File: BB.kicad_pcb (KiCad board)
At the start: 2 copper layers, 0 parts

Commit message: Added Relay module footprints.
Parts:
- added D1: LG Q971-KN-1, LEDs:LED-0603, F.Cu at (300.1, 95.9)
- added D2: B130-13-F, BB:SMA, F.Cu at (296.7, 104.0)
- added K1: 1461069-5, BB:TE-SPDT, F.Cu at (306.4, 96.6)
- added Q1: 2N3904, SMD_Packages:SOT23EBC, B.Cu at (304.5, 103.4)
- added R1: 500, SMD_Packages:SM0805, F.Cu at (290.6, 90.9)
- added R2: 200, SMD_Packages:SM0805, F.Cu at (300.6, 99.7)
- added R3: 100, SMD_Packages:SM0805, B.Cu at (307.0, 93.6)
- added R4: 0, SMD_Packages:SM0805, B.Cu at (305.4, 89.3)
- added R5: 0, SMD_Packages:SM0805, B.Cu at (312.5, 90.0)
- added R6: 0, SMD_Packages:SM0805, B.Cu at (304.3, 99.2)
- added U1: LTV-816S, BB:4-SMD, F.Cu at (293.2, 90.2)
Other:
- board outline added: 165.1 x 63.5 mm
- copper layers 2 -> 4
- rule pad_to_mask_clearance: 0 -> 0.127
- rule trace_min: 0.254 -> 0.1524
- rule via_min_drill: 0.508 -> 0.3302
- rule via_min_size: 0.889 -> 0.508

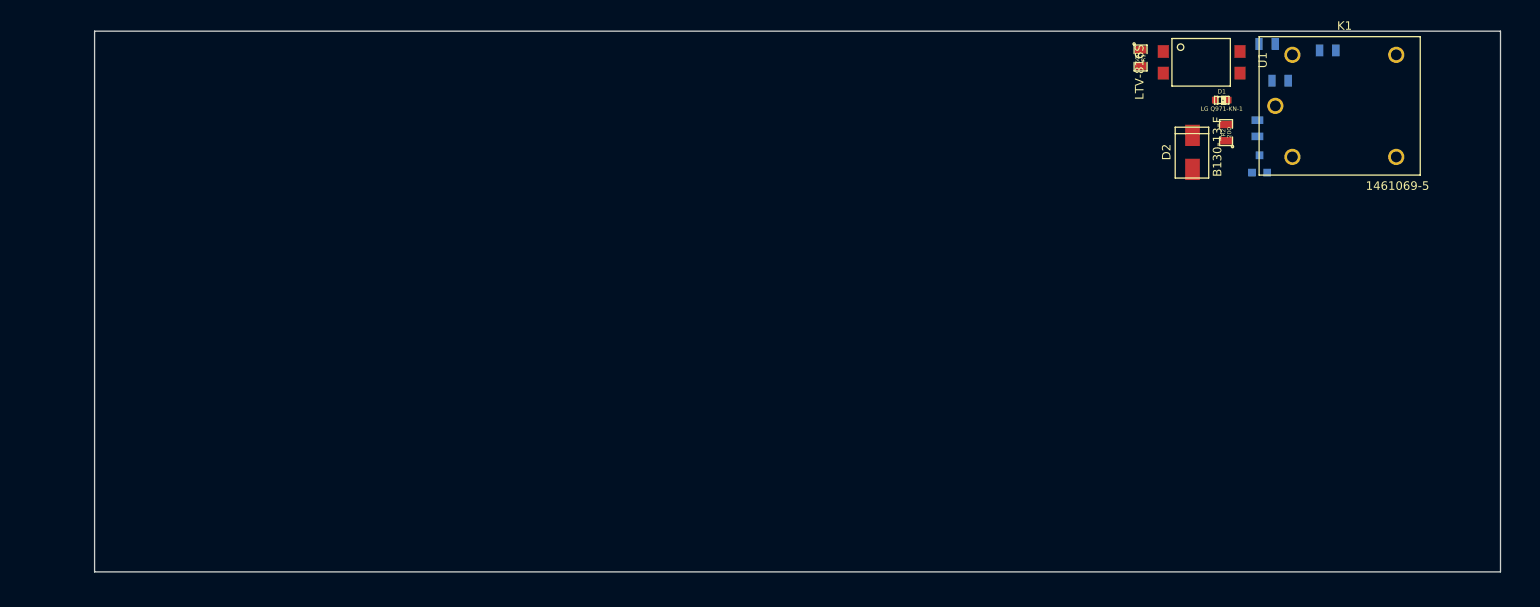
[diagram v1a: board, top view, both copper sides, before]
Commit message: Associated and placed thermocouple, terminal, arduino, fan driver, power protection modules.
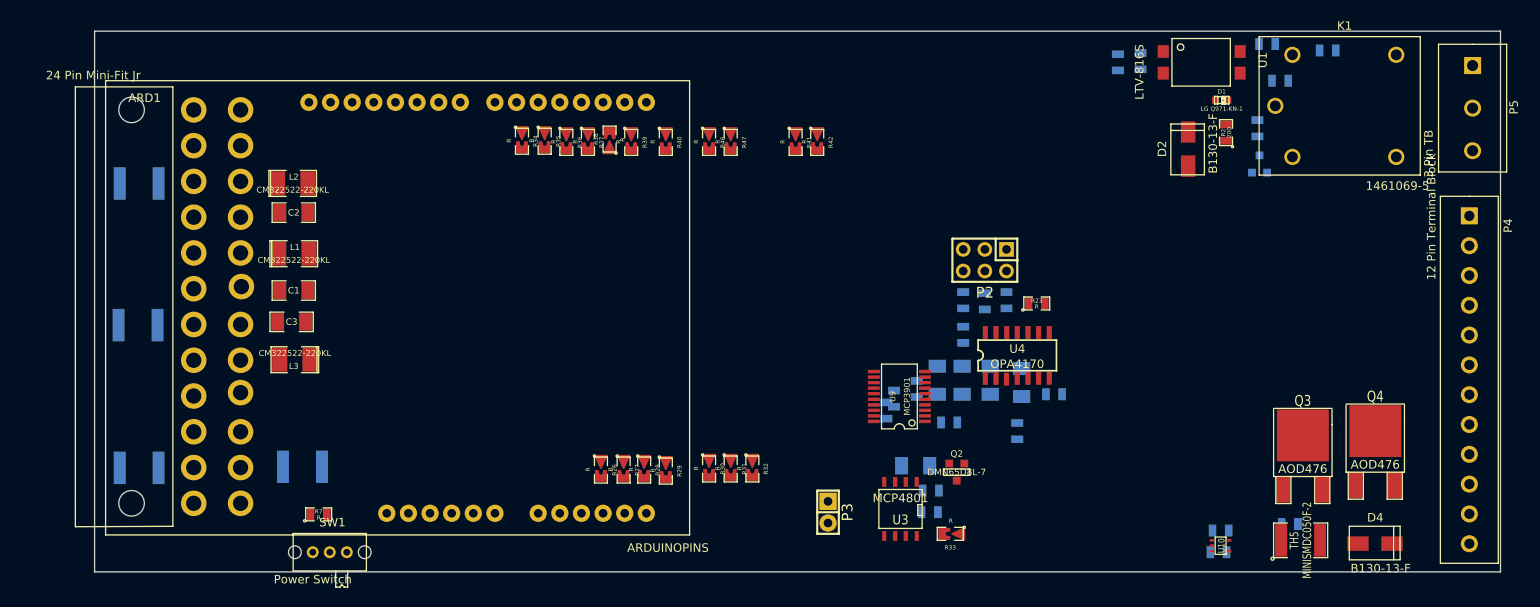
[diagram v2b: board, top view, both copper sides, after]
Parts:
- added ARD1: ARDUINOPINS, BB:Arduino, F.Cu at (203.6, 120.5)
- added C1: C, SMD_Packages:SM1206, F.Cu at (191.1, 118.2)
- added C10: C, SMD_Packages:SM0805, B.Cu at (276.1, 134.7)
- added C11: C, SMD_Packages:SM0805, B.Cu at (299.7, 149.0)
- added C12: C, SMD_Packages:SM0805, B.Cu at (265.9, 141.7)
- added C13: C, SMD_Packages:SM0805, B.Cu at (308.1, 145.7)
- added C2: C, SMD_Packages:SM1206, F.Cu at (191.1, 109.1)
- added C3: C, SMD_Packages:SM1206, F.Cu at (190.9, 121.9)
- added C6: C, SMD_Packages:SM0805, B.Cu at (264.3, 129.8)
- added C7: C, SMD_Packages:SM0805, B.Cu at (261.6, 130.9)
- added C8: C, SMD_Packages:SM0805, B.Cu at (260.7, 132.3)
- added C9: C, SMD_Packages:SM0805, B.Cu at (280.4, 130.4)
- added D4: B130-13-F, BB:SMA, F.Cu at (316.1, 148.0)
- added L1: CM322522-220KL, SMD_Packages:SM1210L, F.Cu at (191.1, 113.9)
- added L2: CM322522-220KL, SMD_Packages:SM1210L, F.Cu at (191.0, 105.7)
- added L3: CM322522-220KL, SMD_Packages:SM1210L, F.Cu at (191.3, 126.4)
- added P1: 24 Pin Mini-Fit Jr, BB:ATX_Header, F.Cu at (172.1, 97.0)
- added P2: CONN_3X2, BB:Pin_Header_Straight_3X2, F.Cu at (272.3, 114.7)
- added P3: CONN_2, Pin_Headers:Pin_Header_Straight_1x02, F.Cu at (253.9, 144.3)
- added P4: 12 Pin Terminal Block, BB:12PinTB, F.Cu at (329.2, 109.5)
- added P5: 3 Pin TB, BB:3PinTB, F.Cu at (329.6, 91.8)
- added Q2: DMN65D8L-7, SMD_Packages:SOT23GDS, F.Cu at (269.0, 139.6)
- added Q3: AOD476, SMD_Packages:DPAK2, F.Cu at (309.6, 141.6)
- added Q4: AOD476, SMD_Packages:DPAK2, F.Cu at (318.1, 141.1)
- added R10: R, SMD_Packages:SM1206, B.Cu at (264.2, 138.8)
- added R19: R, SMD_Packages:SM1206, B.Cu at (276.6, 129.0)
- added R20: R, SMD_Packages:SM1206, B.Cu at (266.7, 128.8)
- added R21: R, SMD_Packages:SM1206, B.Cu at (272.9, 128.8)
- added R22: R, SMD_Packages:SM1206, B.Cu at (269.6, 128.8)
- added R23: R, SMD_Packages:SM0805, F.Cu at (278.4, 119.8)
- added R24: R, SMD_Packages:SM0805, B.Cu at (269.7, 119.4)
- added R25: R, SMD_Packages:SM0805, B.Cu at (269.7, 123.4)
- added R26: R, BB:SM0805-blob, F.Cu at (227.2, 139.3)
- added R27: R, BB:SM0805-blob, F.Cu at (229.9, 139.3)
- added R28: R, BB:SM0805-blob, F.Cu at (232.3, 139.3)
- added R29: R, BB:SM0805-blob, F.Cu at (234.8, 139.4)
- added R30: R, BB:SM0805-blob, F.Cu at (239.9, 139.2)
- added R31: R, BB:SM0805-blob, F.Cu at (242.4, 139.2)
- added R32: R, BB:SM0805-blob, F.Cu at (245.0, 139.2)
- added R33: R, BB:SM0805-blob, F.Cu at (268.2, 146.8)
- added R34: R, BB:SM0805-blob, F.Cu at (217.9, 100.7)
- added R35: R, BB:SM0805-blob, F.Cu at (220.6, 100.7)
- added R36: R, BB:SM0805-blob, F.Cu at (223.1, 100.8)
- added R37: R, BB:SM0805-blob, F.Cu at (225.7, 100.8)
- added R38: R, BB:SM0805-blob, F.Cu at (228.2, 100.5)
- added R39: R, BB:SM0805-blob, F.Cu at (230.8, 100.8)
- added R40: R, BB:SM0805-blob, F.Cu at (234.8, 100.8)
- added R41: R, BB:SM0805-blob, F.Cu at (250.1, 100.8)
- added R42: R, BB:SM0805-blob, F.Cu at (252.6, 100.8)
- added R43: R, SMD_Packages:SM0805, B.Cu at (287.9, 91.4)
- added R44: R, SMD_Packages:SM0805, B.Cu at (272.3, 119.5)
- added R45: R, SMD_Packages:SM0805, B.Cu at (274.8, 119.4)
- added R46: R, BB:SM0805-blob, F.Cu at (239.9, 100.8)
- added R47: R, BB:SM0805-blob, F.Cu at (242.4, 100.8)
- added R48: 0, SMD_Packages:SM0805, B.Cu at (300.0, 146.4)
- added R49: 0, SMD_Packages:SM0805, B.Cu at (268.1, 133.7)
- added R7: R, SMD_Packages:SM0805, F.Cu at (194.1, 144.5)
- added R9: R, SMD_Packages:SM0805, B.Cu at (265.8, 144.3)
- added SW1: Power Switch, BB:BB_Switch, F.Cu at (191.3, 149.0)
- added TH1: MINISMDC050F-2, SMD_Packages:SM1812, B.Cu at (173.0, 139.1)
- added TH2: MINISMDC050F-2, SMD_Packages:SM1812, B.Cu at (172.8, 122.3)
- added TH3: MINISMDC050F-2, SMD_Packages:SM1812, B.Cu at (173.0, 105.7)
- added TH4: MINISMDC050F-2, SMD_Packages:SM1812, B.Cu at (192.2, 138.9)
- added TH5: MINISMDC050F-2, SMD_Packages:SM1812, F.Cu at (309.4, 147.6)
- added U10: LMT84, SMD_Packages:SOT353, F.Cu at (300.0, 148.2)
- added U3: MCP4801, SMD_Packages:SO8N, F.Cu at (262.4, 143.9)
- added U4: OPA4170, SOIC_Packages:SOIC-14_Narrow, F.Cu at (276.1, 125.9)
- added U9: MCP3901, SSOP_Packages:SSOP-20, F.Cu at (262.3, 130.7)
- R1: moved to B.Cu
- moved D2 0.64 mm to (296.2, 103.6)
- moved R1 0.38 mm to (290.6, 91.3)

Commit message: Layout sessions 1-4.
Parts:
- added 3_mm: VAL**, BB:3_mm, F.Cu at (212.7, 67.9)
- added 3_mm: VAL**, BB:3_mm, F.Cu at (71.6, 66.5)
- added 3_mm: VAL**, BB:3_mm, F.Cu at (71.6, 122.9)
- added C14: C, SMD_Packages:SM0805, B.Cu at (198.8, 151.5)
- added C15: C, SMD_Packages:SM0805, B.Cu at (187.9, 162.9)
- added C16: C, SMD_Packages:SM0805, B.Cu at (188.8, 160.0)
- added C17: C, SMD_Packages:SM0805, B.Cu at (191.8, 156.1)
- added C18: C, SMD_Packages:SM0805, B.Cu at (199.2, 136.7)
- added C19: C, SMD_Packages:SM0805, B.Cu at (181.8, 166.1)
- added C20: C, SMD_Packages:SM0805, B.Cu at (197.5, 141.4)
- added C21: C, SMD_Packages:SM0805, B.Cu at (184.8, 164.5)
- added C22: C, SMD_Packages:SM0805, B.Cu at (197.8, 156.7)
- added C23: C, SMD_Packages:SM0805, B.Cu at (194.4, 157.4)
- added C24: C, SMD_Packages:SM0805, B.Cu at (192.0, 160.2)
- added C25: C, SMD_Packages:SM0805, B.Cu at (185.7, 167.7)
- added C4: 1u, SMD_Packages:SM0805, B.Cu at (167.1, 103.6)
- added C5: 1u, SMD_Packages:SM0805, B.Cu at (169.9, 103.4)
- added D10: MMBD914-7-F, BB:SOT23-DIODE, F.Cu at (142.8, 163.8)
- added D11: MMBD914-7-F, BB:SOT23-DIODE, F.Cu at (153.8, 163.8)
- added D12: MMBD914-7-F, BB:SOT23-DIODE, F.Cu at (165.7, 166.1)
- added D13: MMBD914-7-F, BB:SOT23-DIODE, F.Cu at (146.0, 167.4)
- added D3: B0540WS-7, BB:SOD-323, F.Cu at (165.1, 104.6)
- added D6: MMBD914-7-F, BB:SOT23-DIODE, F.Cu at (153.4, 167.4)
- added D7: MMBD914-7-F, BB:SOT23-DIODE, F.Cu at (193.8, 137.5)
- added D8: MMBD914-7-F, BB:SOT23-DIODE, F.Cu at (191.5, 142.8)
- added D9: MMBD914-7-F, BB:SOT23-DIODE, F.Cu at (174.9, 166.1)
- added JP1: JUMPER, Pin_Headers:Pin_Header_Straight_2x01, F.Cu at (190.8, 151.3)
- added L4: 22u, BB:NR4012, F.Cu at (159.6, 103.8)
- added R11: 5K, BB:EVUE3K, F.Cu at (130.2, 67.3)
- added R12: 715, SMD_Packages:SM0805, B.Cu at (198.0, 144.3)
- added R13: 715, SMD_Packages:SM0805, B.Cu at (197.0, 154.5)
- added R14: 5K, BB:EVUE3K, F.Cu at (107.4, 67.4)
- added R15: R, SMD_Packages:SM0805, B.Cu at (181.5, 163.7)
- added R16: R, SMD_Packages:SM0805, B.Cu at (199.9, 139.7)
- added R17: R, SMD_Packages:SM0805, B.Cu at (197.5, 147.6)
- added R18: R, SMD_Packages:SM0805, B.Cu at (188.6, 155.3)
- added R50: R, BB:SM0805-blob, F.Cu at (140.8, 81.4)
- added R51: R, BB:SM0805-blob, F.Cu at (143.4, 81.4)
- added R52: R, SMD_Packages:SM0805, B.Cu at (180.9, 169.0)
- added R53: R, SMD_Packages:SM0805, F.Cu at (196.1, 151.5)
- added R54: R, SMD_Packages:SM0805, B.Cu at (200.0, 147.6)
- added R55: R, SMD_Packages:SM0805, F.Cu at (188.8, 157.6)
- added R8: 15, SMD_Packages:SM0805, B.Cu at (172.2, 103.4)
- added U2: AP5726, SMD_Packages:SOT23_6, F.Cu at (169.4, 103.1)
- added U5: LM337T, Discret:TO220_VERT, F.Cu at (160.7, 70.2)
- added U6: LM337T, Discret:TO220_VERT, F.Cu at (202.4, 73.7)
- added U7: LM317_BB, Discret:TO220_VERT, F.Cu at (175.8, 70.4)
- added U8: LM317_BB, Discret:TO220_VERT, F.Cu at (189.5, 73.7)
- added V8508: VAL**, BB:V8508, F.Cu at (175.6, 65.4)
- added V8508: VAL**, BB:V8508, F.Cu at (160.7, 65.2)
- C1, L1, TH5: moved to B.Cu
- moved C12 169.6 mm to (132.6, 37.0)
- moved Q2 169.6 mm to (135.6, 34.8)
- moved R10 169.6 mm to (130.8, 34.0)
- moved R9 169.6 mm to (132.5, 39.5)
- moved C7 145.5 mm to (161.3, 25.5)
- moved C6 145.5 mm to (164.0, 24.4)
- moved R20 143.6 mm to (166.9, 25.5)
- moved C8 142.0 mm to (161.9, 30.4)
- moved Q4 138.1 mm to (189.0, 92.2), turned to 90 degrees
- moved L1 134.5 mm to (61.1, 79.8), turned to 90 degrees
- moved C1 132.4 mm to (64.4, 79.9), turned to 270 degrees
- moved TH5 132.4 mm to (189.1, 92.3), turned to 90 degrees
- moved R5 132.3 mm to (183.1, 117.3)
- moved P3 132.1 mm to (129.2, 100.6)
- moved R33 132.0 mm to (140.5, 113.8), turned to 270 degrees
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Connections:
- net +12V renamed FE_V+
- C11 pad 2: Net-(C11-Pad2) -> AGND
- C9 pad 2: -12V -> FE_V-
- K1 pad 3: /Relay/RELAY_NO -> /Relay/RELAY_NC
- K1 pad 4: /Relay/RELAY_NC -> /Relay/RELAY_NO
- P1 pad 2: Net-(P1-Pad2) -> Net-(P1-Pad12)
- P4 pad 1: +3.3V -> /LED_Driver/LED_STRING+
- P4 pad 10: /Fan/TACH_IN -> +3.3V
- P4 pad 11: /TerminalBlock/TC_IN+ -> /PowerAdjustmentMonitor/V-_ADJ
- P4 pad 12: /TerminalBlock/TC_IN- -> /PowerAdjustmentMonitor/V+_ADJ
- P4 pad 2: +5V -> /LED_Driver/LED_STRING-
- P4 pad 3: GND -> /Fan/TACH_IN
- P4 pad 4: /TerminalBlock/V+_ADJ -> /Fan/FAN_OUT-
- P4 pad 5: /TerminalBlock/V-_ADJ -> /Fan/FAN_OUT+
- P4 pad 6: /LED_Driver/LED_STRING+ -> /TerminalBlock/TC_IN-
- P4 pad 7: /LED_Driver/LED_STRING- -> /TerminalBlock/TC_IN+
- P4 pad 8: /Fan/FAN_OUT+ -> GND_PWR
- P4 pad 9: /Fan/FAN_OUT- -> +5V
- P5 pad 1: /Relay/RELAY_NC -> /Relay/RELAY_NO
- P5 pad 3: /Relay/RELAY_NO -> /Relay/RELAY_NC
- R2 pad 1: GND -> GND_RELAY
- R6 pad 1: GND -> GND_RELAY
- R9 pad 2: Net-(R9-Pad2) -> Net-(Q2-PadD)
- TH1 pad 1: Net-(P1-Pad2) -> Net-(P1-Pad12)
- TH1 pad 2: +3.3VP -> +3.3V
- U3 pad 7: Net-(U3-Pad7) -> AGND
- U4 pad 11: -12V -> FE_V-
- U4 pad 5: Net-(R9-Pad2) -> Net-(Q2-PadD)
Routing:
- net /Relay/RELAY_COM: track 0.00 -> 22.9 mm
- net AGND: track 0.00 -> 9.26 mm, vias 0 -> 2
- net /Relay/RELAY_NO: track 0.00 -> 9.16 mm
- net /Relay/RELAY_NC: track 0.00 -> 9.09 mm
- net GND_LED: track 0.00 -> 3.62 mm, vias 0 -> 1
- net +5P: track 0.00 -> 2.77 mm, vias 0 -> 1
- net GND_RELAY: track 0.00 -> 2.41 mm, vias 0 -> 1
- added copper zone on PWR, net +5P
- added copper zone on PWR, net +5V
- added copper zone on GND, net AGND
- added copper zone on GND, net GND_LED
- added copper zone on GND, net GND_PWR
- added copper zone on GND, net GND_RELAY
